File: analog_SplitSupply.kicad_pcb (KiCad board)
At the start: 2 copper layers, 79.8 x 67.6 mm, 46 parts, among them J1 Conn_01x04, J2 Conn_01x02, J3 Conn_01x02, J4 Conn_01x02, J5 Conn_01x02, U1 TI_LM2734ZMK_NOPB, U2 AD_LT1054CS8#TRPBF, U3 TI_TLV1117CDCY, U4 AD_LT1175CS8#PBF

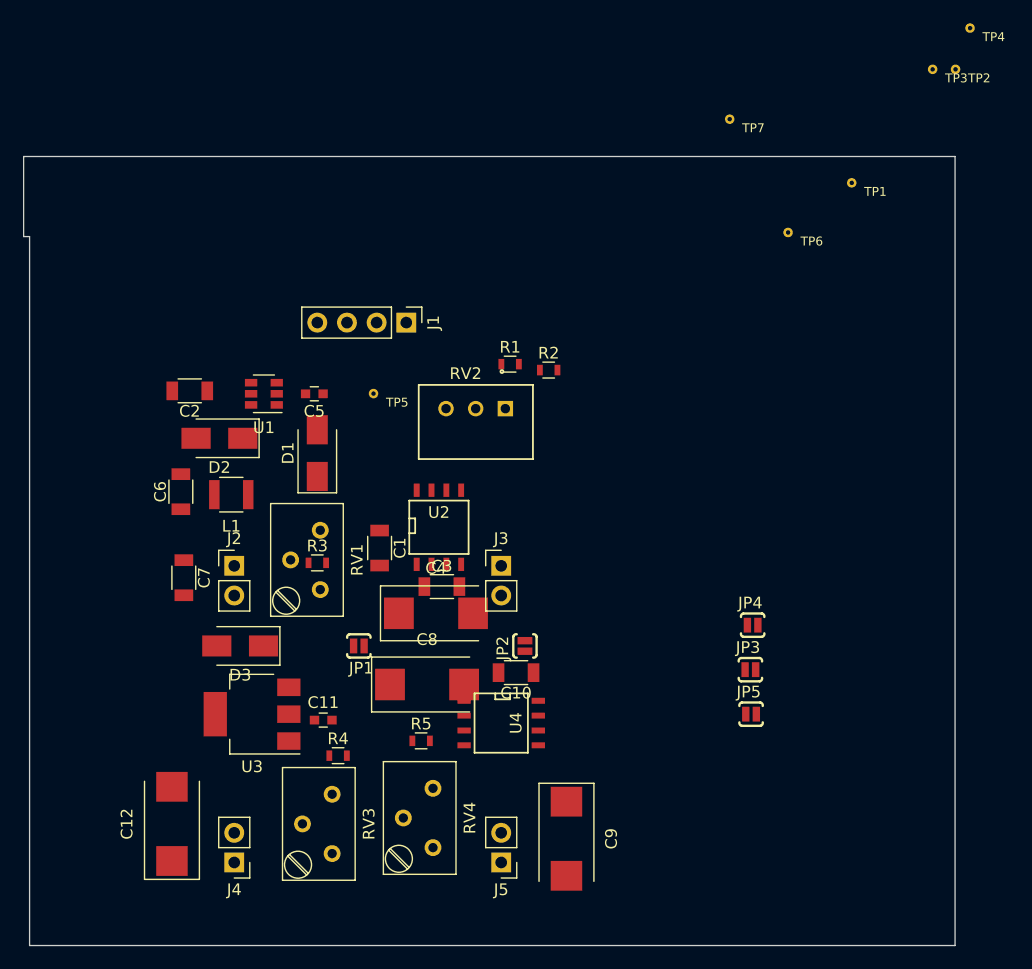
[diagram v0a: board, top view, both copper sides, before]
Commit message: Updated schematic and prelim layout
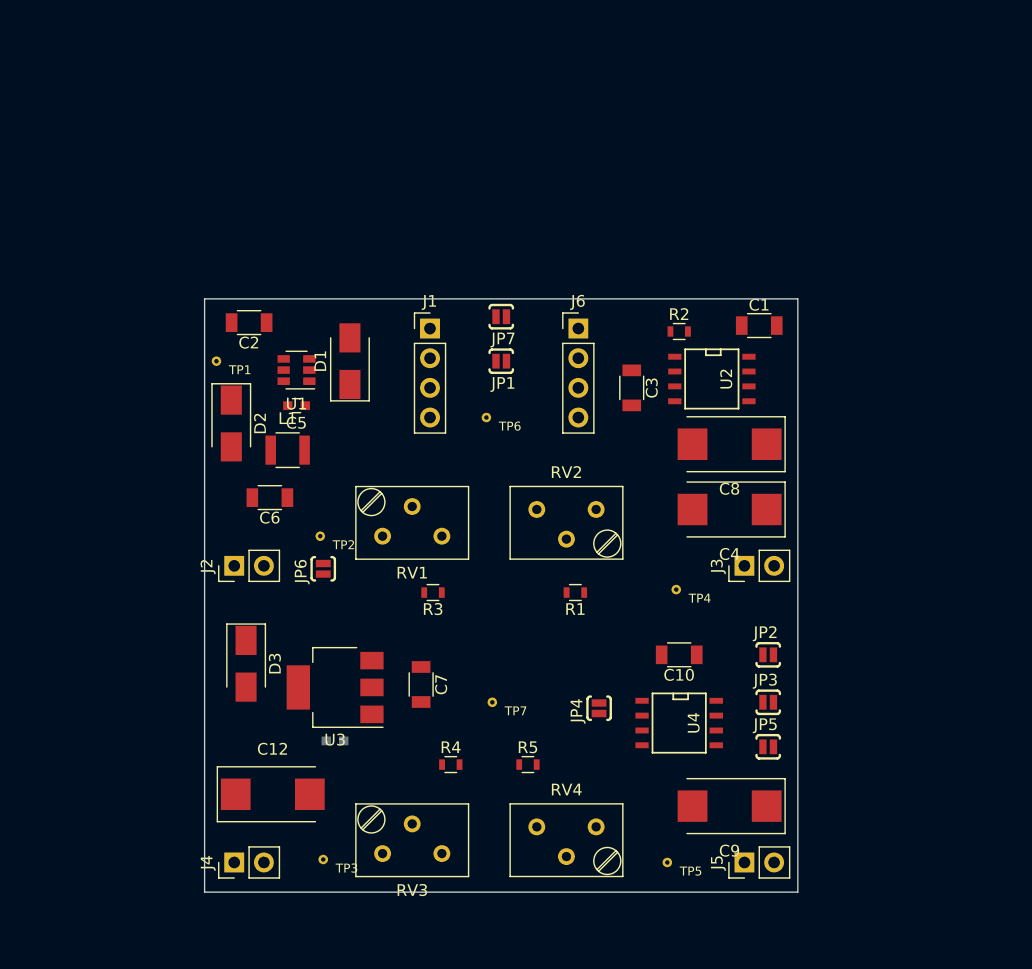
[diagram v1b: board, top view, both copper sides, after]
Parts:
- added J6: Conn_01x04, Pin_Headers:Pin_Header_Straight_1x04_Pitch2.54mm, F.Cu at (131.1, 81.3)
- added JP6: PAD_JUMPER_2PIN_NC, DBLS_Misc:PAD_JUMPER_2PIN_NC, F.Cu at (109.2, 101.9)
- added JP7: PAD_JUMPER_2PIN_NC, DBLS_Misc:PAD_JUMPER_2PIN_NC, F.Cu at (124.5, 80.3)
- C11: moved to B.Cu
- RV2: value BOURNS_3299W-1-204LF -> BOURNS_PV37W204C01B00; footprint DBLS_Resistor:BOURNS_3299W -> Potentiometers:Potentiometer_Trimmer_Bourns_3299Y
- moved TP3 85.4 mm to (109.2, 126.7)
- moved TP2 67.5 mm to (109.0, 99.1)
- moved TP1 56.5 mm to (100.1, 84.1)
- moved TP4 54.3 mm to (139.4, 103.6)
- moved TP7 53.9 mm to (123.7, 113.3)
- moved TP5 47.4 mm to (138.7, 127.0)
- moved C1 37.7 mm to (146.6, 81.0), turned to 0 degrees
- moved C8 33.1 mm to (144.0, 91.2), turned to 180 degrees
- moved TP6 30.3 mm to (123.2, 88.9)
- moved JP1 27.3 mm to (124.5, 84.1)
- moved C4 26.7 mm to (144.0, 96.8), turned to 180 degrees
- moved U2 26.6 mm to (142.5, 85.6), turned to 270 degrees
- moved C3 23.5 mm to (135.6, 86.4), turned to 270 degrees
- moved C7 22.3 mm to (117.6, 111.8)
- moved JP2 20.8 mm to (147.3, 109.2), turned to 180 degrees
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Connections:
- net Net-(C1-Pad1) renamed /VPOS_INV_IN
- net Net-(C10-Pad1) renamed /VNEG_LDO_IN
- C7 pad 1: VSW+ -> /VPOS_LDO_IN
- D3 pad 1: VSW+ -> /VPOS_LDO_IN
- U3 pad 3: VSW+ -> /VPOS_LDO_IN
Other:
- board size 79.8 x 67.6 mm -> 50.8 x 50.8 mm

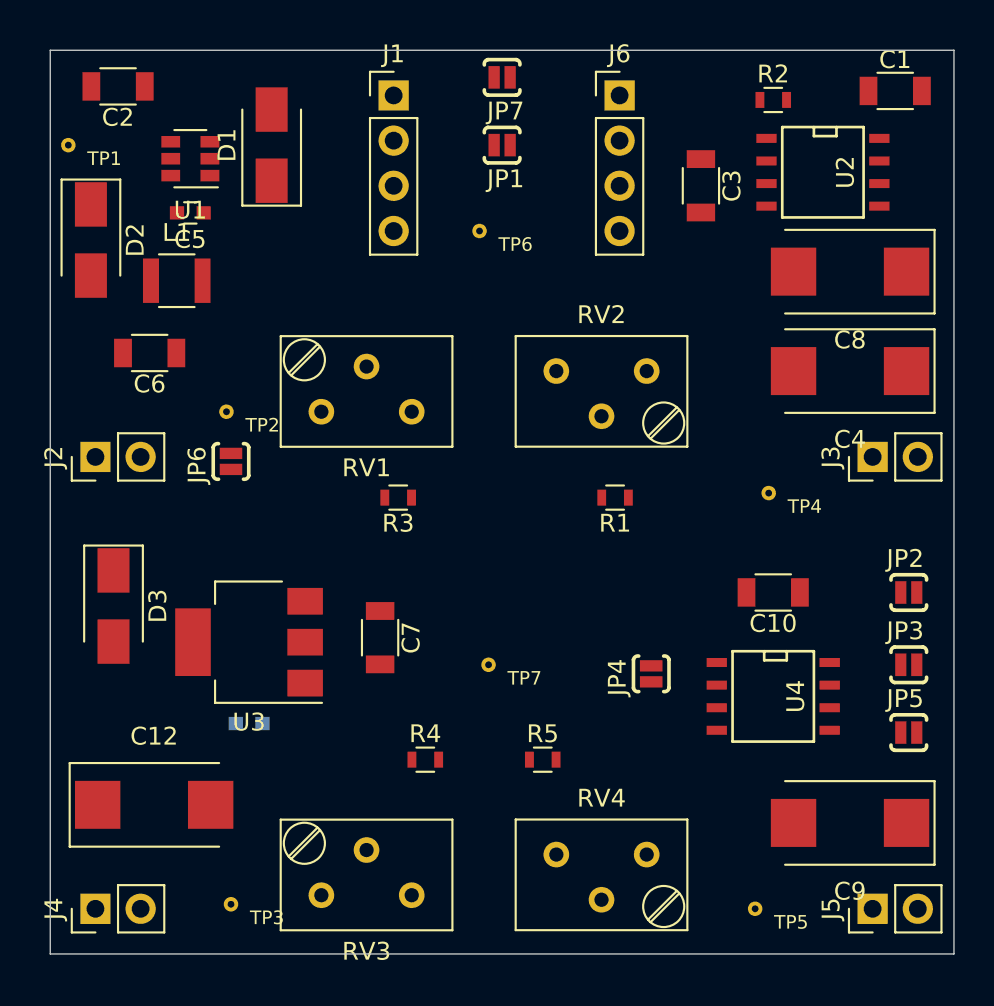
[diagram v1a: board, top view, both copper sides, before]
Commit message: first route awaiting silkscreen cleanup
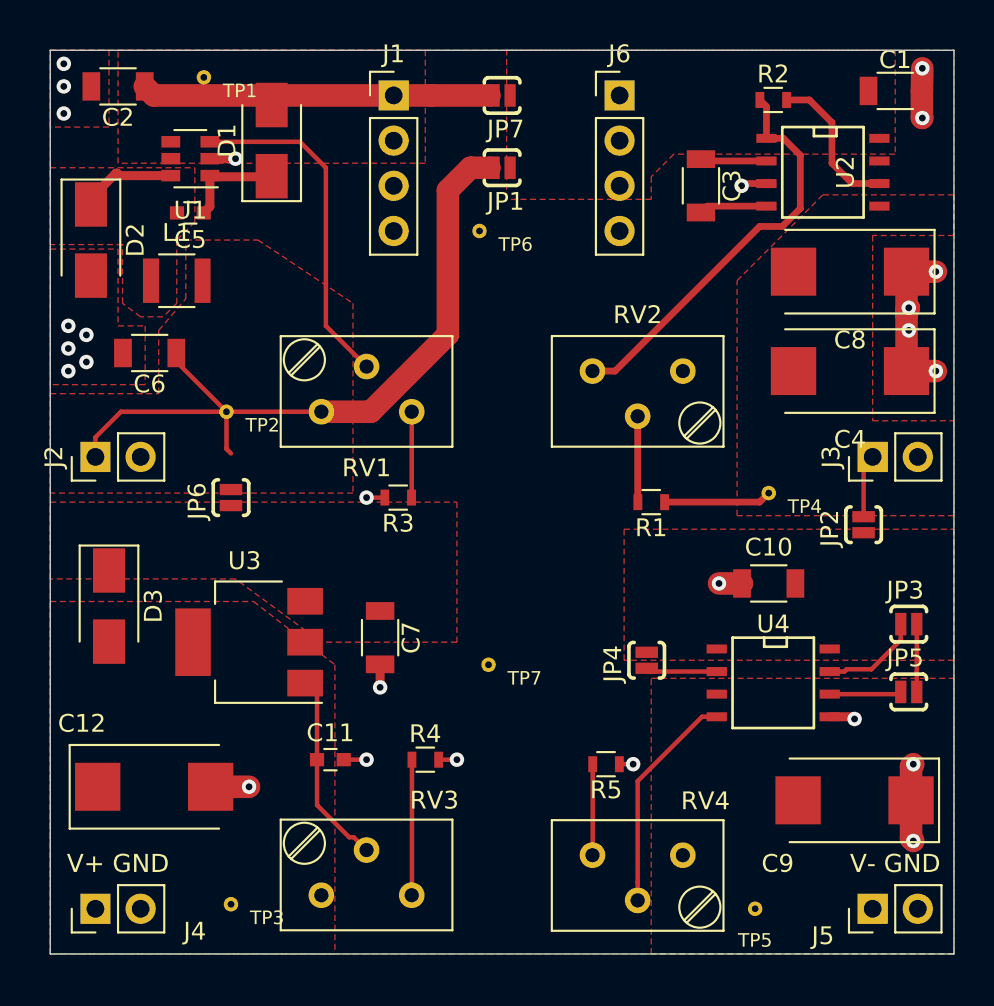
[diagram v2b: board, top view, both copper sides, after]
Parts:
- C11: moved to F.Cu
- moved TP1 8.52 mm to (107.7, 80.3)
- moved C11 5.00 mm to (114.8, 118.6), turned to 0 degrees
- moved JP2 4.58 mm to (144.8, 105.4), turned to 270 degrees
- moved R5 3.57 mm to (130.3, 118.9), turned to 180 degrees
- moved JP3 2.29 mm to (147.3, 111.0)
- moved JP5 2.29 mm to (147.3, 114.8)
- moved R1 2.05 mm to (132.8, 104.1)
- moved RV4 2.03 mm to (134.6, 124.0)
- moved RV2 2.03 mm to (134.6, 96.8)
- moved JP6 2.03 mm to (109.2, 103.9)
- moved C9 1.30 mm to (144.3, 120.9)
- moved JP1 1.27 mm to (124.5, 85.3)
- moved C12 1.02 mm to (104.9, 120.1)
- moved JP7 1.02 mm to (124.5, 81.3)
- moved JP4 0.80 mm to (132.6, 113.0)
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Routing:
- net VSW+: track 0.00 -> 41.2 mm
- net GND: track 0.00 -> 29.6 mm, vias 0 -> 26
- net Net-(R2-Pad1): track 0.00 -> 23.1 mm
- net VIN: track 0.00 -> 19.6 mm
- net Net-(RV1-Pad2): track 0.00 -> 19.2 mm
- net Net-(RV4-Pad2): track 0.00 -> 12.6 mm
- net Net-(C11-Pad1): track 0.00 -> 11.0 mm
- net VSW-: track 0.00 -> 9.64 mm
- net Net-(R2-Pad2): track 0.00 -> 8.50 mm
- net Net-(R4-Pad1): track 0.00 -> 7.62 mm
- net Net-(C5-Pad1): track 0.00 -> 5.83 mm
- net Net-(JP3-Pad2): track 0.00 -> 5.62 mm
- net Net-(C5-Pad2): track 0.00 -> 5.48 mm
- net Net-(R5-Pad2): track 0.00 -> 5.12 mm
- net Net-(R1-Pad2): track 0.00 -> 4.83 mm
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- added copper zone on F.Cu, net /VNEG_LDO_IN
- added copper zone on F.Cu, net /VPOS_INV_IN
- added copper zone on F.Cu, net /VPOS_LDO_IN
- added copper zone on B.Cu, net GND
- added copper zone on F.Cu, net GND
- added copper zone on F.Cu, net Net-(C5-Pad2)
- added copper zone on F.Cu, net V+
- added copper zone on F.Cu, net V-
- added copper zone on F.Cu, net VIN
- added copper zone on F.Cu, net VSW+
- added copper zone on F.Cu, net VSW-
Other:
- net class Default: clearance 0.2 -> 0.2032; trace_width 0.25 -> 0.254; via_dia 0.8 -> 0.8128; via_drill 0.4 -> 0.381
- rule trace_clearance: 0.2 -> 0.2032
- board text added: "V+ GND"
- board text added: "V- GND"

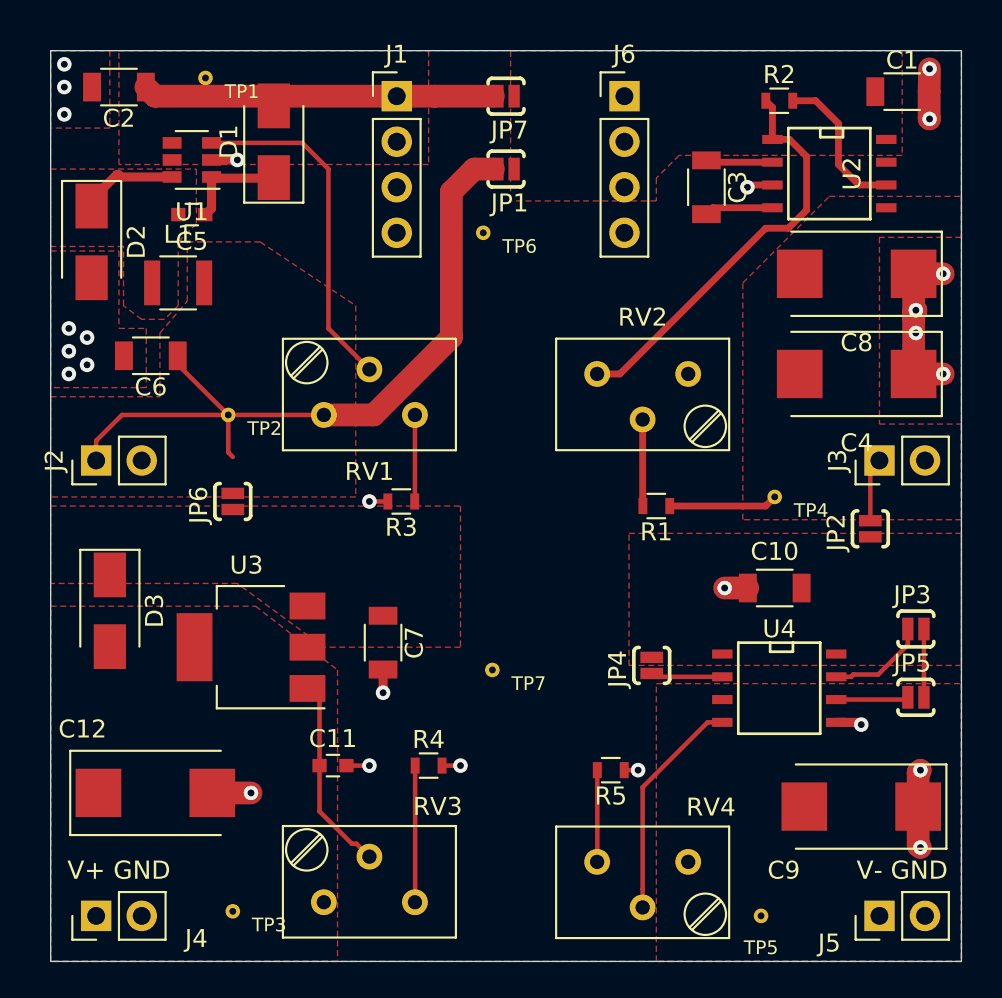
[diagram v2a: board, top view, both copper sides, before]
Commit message: cleaned up silkscreen
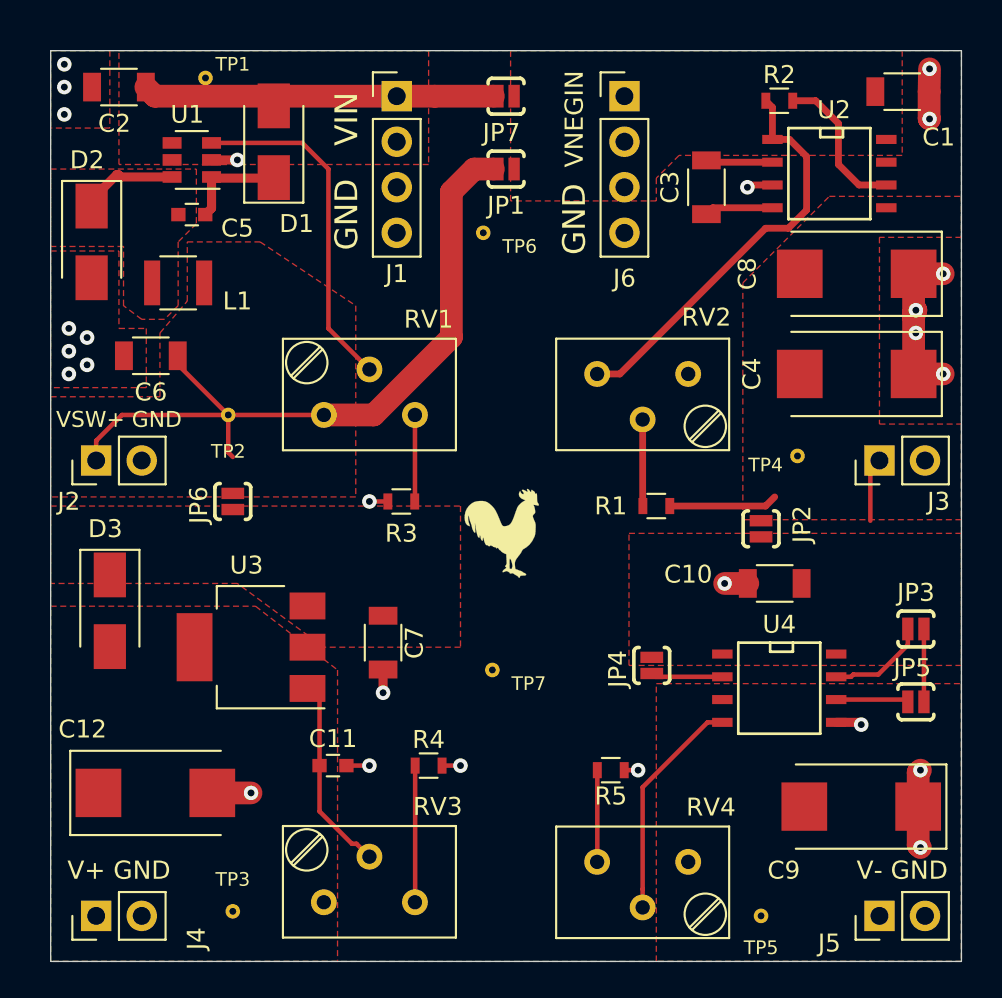
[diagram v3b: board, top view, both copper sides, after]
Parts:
- added LOGO1: DBLS_van_logo_small_v1, DBLS_LOGO:van_logo_small, B.Cu at (123.2, 115.3)
- added LOGO2: DBLS_Chicken_Small, DBLS_LOGO:Rooster_4mmx4mm, F.Cu at (124.2, 105.7)
- moved JP2 6.10 mm to (138.7, 105.4)
- moved TP4 2.62 mm to (140.7, 101.3)
- moved C10 0.25 mm to (139.4, 108.5)
- moved JP5 0.25 mm to (147.3, 115.1)
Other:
- board text added: "GND"
- board text added: "VIN"
- board text added: "VNEGIN"
- board text added: "VSW+ GND"
